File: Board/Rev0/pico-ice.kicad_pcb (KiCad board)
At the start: 2 copper layers, 22.9 x 61 mm, 105 parts, among them J1 USB_C_Receptacle_USB2.0, J10 2x3_2.54mm_Female, J11 2x3_2.54mm_Female, J3 6X2 Female Header, J4 6X2 Female Header, J5 Conn_ARM_JTAG_SWD_10, J6 6X2 Female Header, J7 6X2 Female Header, J8 6X2 Female Header, J9 BOOT_SEL, SW1 PTS820 J25K SMTR LFS, SW2 PTS820 J25K SMTR LFS, U1 NCP1117ST33T3G, U2 W25Q32JVSSIQ, U3 RP2040, U4 CL9293A12L5M, U5 APS6404L-3SQN-SN, U6 ICE40UP5K-SG48ITR, U8 W25Q32JVSSIQ, Y1 12 MHz

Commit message: Synced the latest design files.
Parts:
- moved C22 2.20 mm to (69.6, 88.3), turned to 180 degrees
- moved R6 0.65 mm to (66.7, 111.5), turned to -90 degrees
- moved R2 0.28 mm to (81.8, 120.5)
- moved R3 0.28 mm to (80.1, 121.0)
- moved R10 0.25 mm to (74.7, 124.7)
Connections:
- net Net-(R4-Pad2) renamed /USB_P
- net Net-(R5-Pad2) renamed /USB_N
- SW1 pad SH1: unconnected-(SW1-PadSH1) -> GND
- SW1 pad SH2: unconnected-(SW1-PadSH2) -> GND
- SW2 pad SH1: unconnected-(SW2-PadSH1) -> GND
- SW2 pad SH2: unconnected-(SW2-PadSH2) -> GND
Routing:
- net +3V3: track 0.00 -> 55.8 mm, vias 0 -> 11
- net /QSPI_SD2: track 0.00 -> 12.1 mm, vias 0 -> 1
- net /QSPI_SD1: track 0.00 -> 11.3 mm, vias 0 -> 1
- net /USB_D-: track 0.00 -> 11.0 mm
- net Net-(J1-PadA4): track 0.00 -> 10.9 mm, vias 0 -> 2
- net /USB_D+: track 0.00 -> 10.2 mm, vias 0 -> 2
- net /QSPI_SD0: track 0.00 -> 9.72 mm, vias 0 -> 1
- net /QSPI_SS: track 0.00 -> 9.24 mm, vias 0 -> 1
- net /QSPI_SCLK: track 0.00 -> 8.38 mm, vias 0 -> 1
- net /QSPI_SD3: track 0.00 -> 6.98 mm, vias 0 -> 1
- net /XIN: track 0.00 -> 6.59 mm
- net +1V1: track 0.00 -> 6.13 mm, vias 0 -> 3
- net Net-(C29-Pad1): track 0.00 -> 5.93 mm
- net GND: track 0.00 -> 5.53 mm, vias 0 -> 2
- net /USB_P: track 0.00 -> 3.62 mm
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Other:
- copper layers 2 -> 4

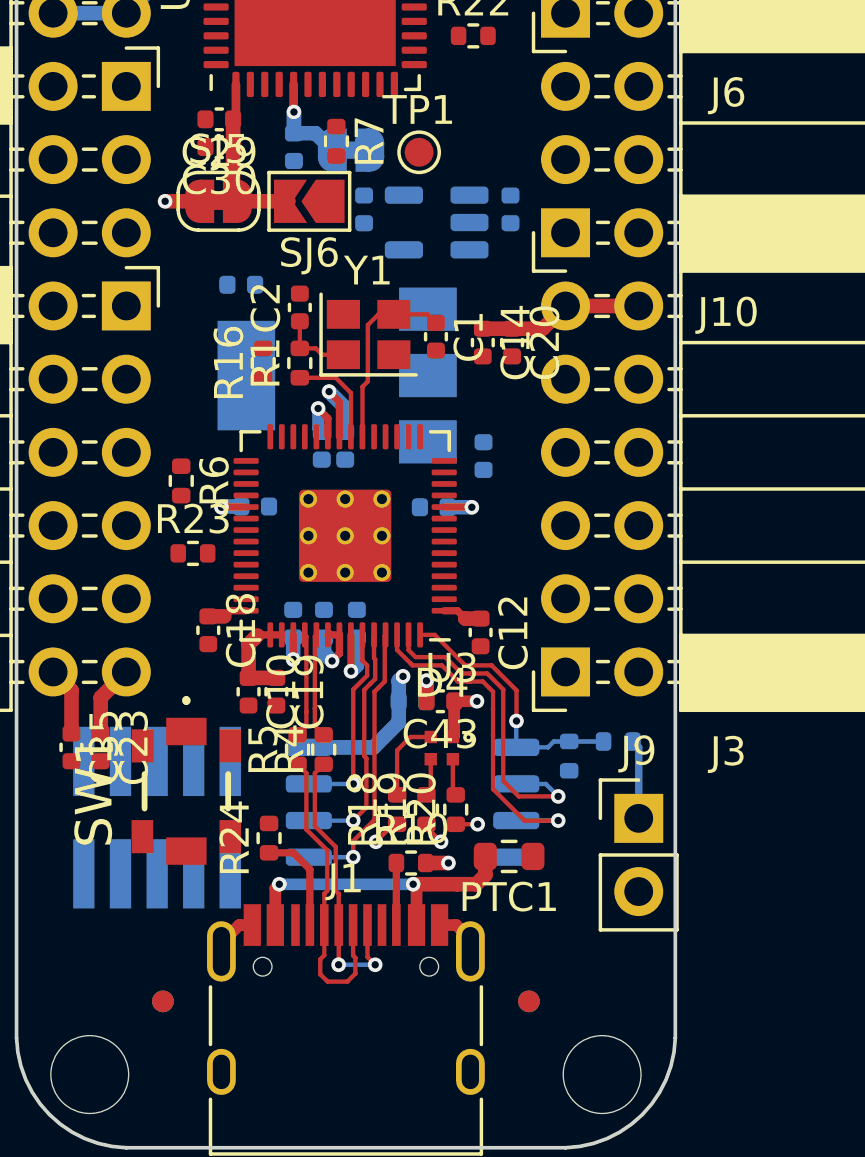
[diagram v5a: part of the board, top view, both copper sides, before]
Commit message: Minor changes to pinouts of headers.
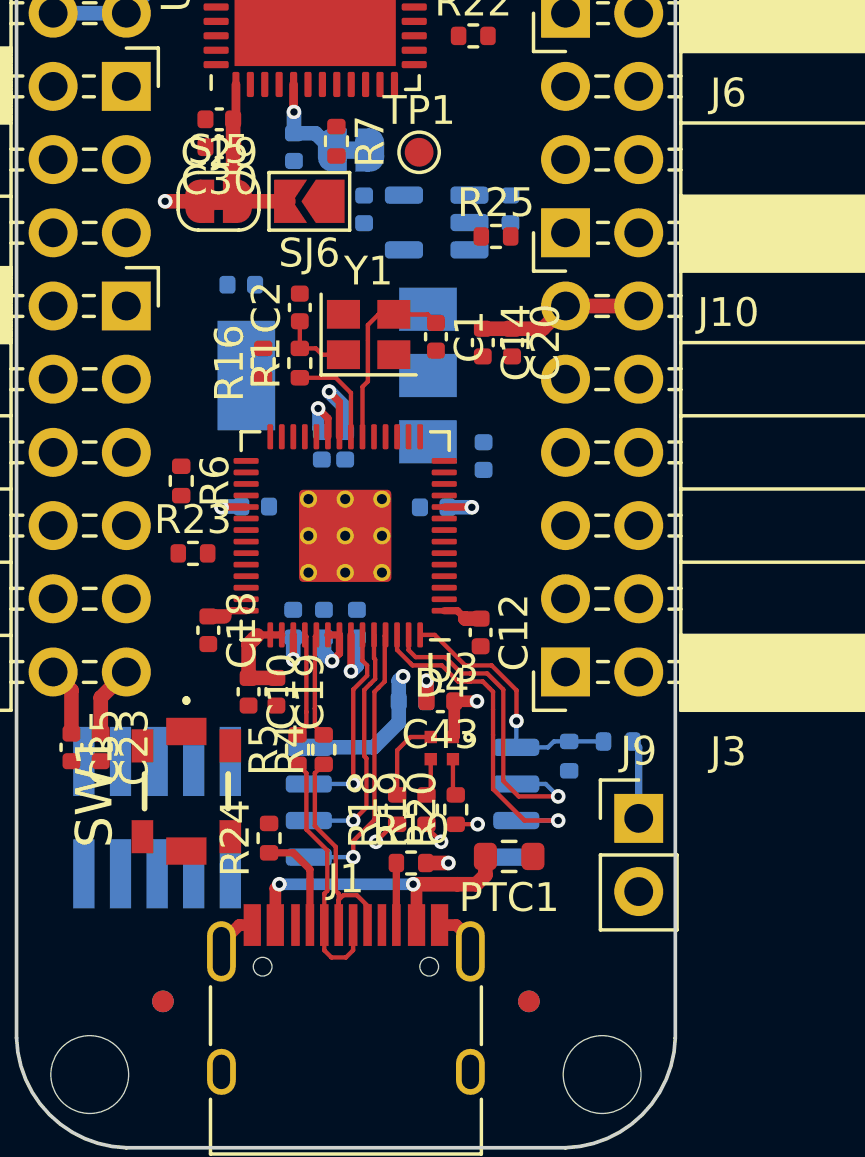
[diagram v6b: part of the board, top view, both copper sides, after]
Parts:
- added R25: 27, Resistor_SMD:R_0402_1005Metric, F.Cu at (77.6, 103.0)
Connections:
- J10 pad 1: /ADC2 -> /ICE_DONE_ADC0
- J10 pad 2: /~{RESET} -> /ADC3
- J10 pad 3: /PICO_CLKOUT -> /ADC2
- J10 pad 4: /ADC3 -> VBUS
- J10 pad 6: VBUS -> /~{RESET}
- J11 pad 1: /ICE_9 -> /PICO_CLKOUT
- J11 pad 2: /ICE_6 -> /ICE_35_G0
- J11 pad 5: /SRAM_SSN -> /ICE_9
- J11 pad 6: /ICE_35_G0 -> /ICE_6
- J7 pad b6: /ICE_DONE -> /SRAM_SSN
- U3 pad 38: /ICE_DONE -> /ICE_DONE_ADC0
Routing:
- net /USB_D-: track 11.0 -> 9.01 mm
- net /USB_D+: track 10.2 -> 8.81 mm, vias 2 -> 0

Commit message: Finished the routing
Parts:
- C15, C16, C17, C5: moved to F.Cu
- moved C5 2.57 mm to (71.5, 107.7), turned to 90 degrees
- moved C16 2.57 mm to (72.4, 107.7), turned to 90 degrees
- moved C15 2.29 mm to (77.7, 112.9), turned to -90 degrees
- moved C17 2.09 mm to (67.2, 112.5), turned to 180 degrees
- moved R1 1.47 mm to (70.8, 105.9)
- moved Y1 1.45 mm to (73.1, 105.0), turned to -90 degrees
- moved C2 1.37 mm to (70.8, 104.1)
- moved C1 1.12 mm to (75.5, 105.4), turned to 90 degrees
- moved R16 1.09 mm to (69.5, 106.3)
- moved R17 1.00 mm to (77.0, 87.6), turned to 0 degrees
- moved C42 0.89 mm to (73.1, 88.9), turned to 180 degrees
- moved TP1 0.72 mm to (75.4, 99.5)
- moved U1 0.46 mm to (72.5, 107.7)
- moved C7 0.38 mm to (69.1, 104.7)
- moved R6 0.28 mm to (66.7, 111.2)
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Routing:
- net GND: track 5.53 -> 103.2 mm, vias 2 -> 34
- net +3V3: track 55.8 -> 141.8 mm, vias 11 -> 23
- net /ICE_SO: track 0.00 -> 71.8 mm, vias 0 -> 3
- net /ICE_SI: track 0.00 -> 60.9 mm, vias 0 -> 3
- net /ICE_SSN: track 0.23 -> 60.3 mm, vias 0 -> 3
- net /SRAM_SSN: track 0.00 -> 56.6 mm, vias 0 -> 4
- net /ICE_18: track 0.00 -> 52.4 mm, vias 0 -> 2
- net /ICE_FLASH_IO3: track 0.00 -> 51.4 mm, vias 0 -> 3
- net /ICE_DONE: track 0.00 -> 49.2 mm, vias 0 -> 2
- net /ICE_20_G3: track 0.00 -> 47.9 mm, vias 0 -> 1
- net /ICE_RSTn: track 0.00 -> 47.6 mm, vias 0 -> 2
- net /ICE_SCK: track 0.00 -> 47.2 mm, vias 0 -> 5
- net /ICE_10|PB: track 0.00 -> 46.2 mm, vias 0 -> 1
- net VBUS: track 0.00 -> 44.6 mm, vias 0 -> 4
- net /ICE_19: track 0.00 -> 43.3 mm, vias 0 -> 2
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- added copper zone on F.Cu, net +3V3
- added copper zone on In2.Cu, net +3V3
- added copper zone on B.Cu, net GND
- added copper zone on F.Cu, net GND
- added copper zone on In1.Cu, net GND
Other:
- board text added: "A"

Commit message: Updated the routing.
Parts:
- moved C15 0.05 mm to (77.6, 112.9)
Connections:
- J10 pad 3: /ADC2 -> VBUS
- J10 pad 4: VBUS -> /ADC2
- J11 pad 1: /PICO_CLKOUT -> /ICE_10|PB
- J11 pad 4: /ICE_10|PB -> /PICO_CLKOUT
- J11 pad 5: /ICE_9 -> /ICE_6
- J11 pad 6: /ICE_6 -> /ICE_9
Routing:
- net VBUS: track 44.6 -> 8.95 mm, vias 4 -> 11
- net /ICE_DONE: track 49.2 -> 77.4 mm, vias 2 -> 5
- net GND: track 103.2 -> 79.8 mm, vias 34 -> 27
- net /ICE_RSTn: track 47.6 -> 70.3 mm
- net /ICE_DONE_ADC0: track 25.0 -> 41.1 mm
- net +3V3: track 141.8 -> 130.5 mm, vias 23 -> 22
- net /ICE_SI: track 60.9 -> 71.1 mm, vias 3 -> 5
- net /VIO_BANK_2: track 28.8 -> 38.1 mm
- net /ICE_35_G0: track 39.4 -> 32.1 mm, vias 3 -> 4
- net +1V2: track 24.4 -> 20.3 mm
- net /ICE_11: track 15.7 -> 19.8 mm
- net /ICE_SSN: track 60.3 -> 64.4 mm
- net /ADC2: track 37.1 -> 41.0 mm, vias 1 -> 3
- net /ICE_10|PB: track 46.2 -> 42.4 mm
- net /ADC3: track 35.1 -> 38.8 mm, vias 1 -> 3
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- added copper zone on B.Cu, net VBUS
- added copper zone on F.Cu, net VBUS
- added copper zone on In2.Cu, net VBUS
